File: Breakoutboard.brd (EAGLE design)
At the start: 17.7 x 25.4 mm, 3 parts

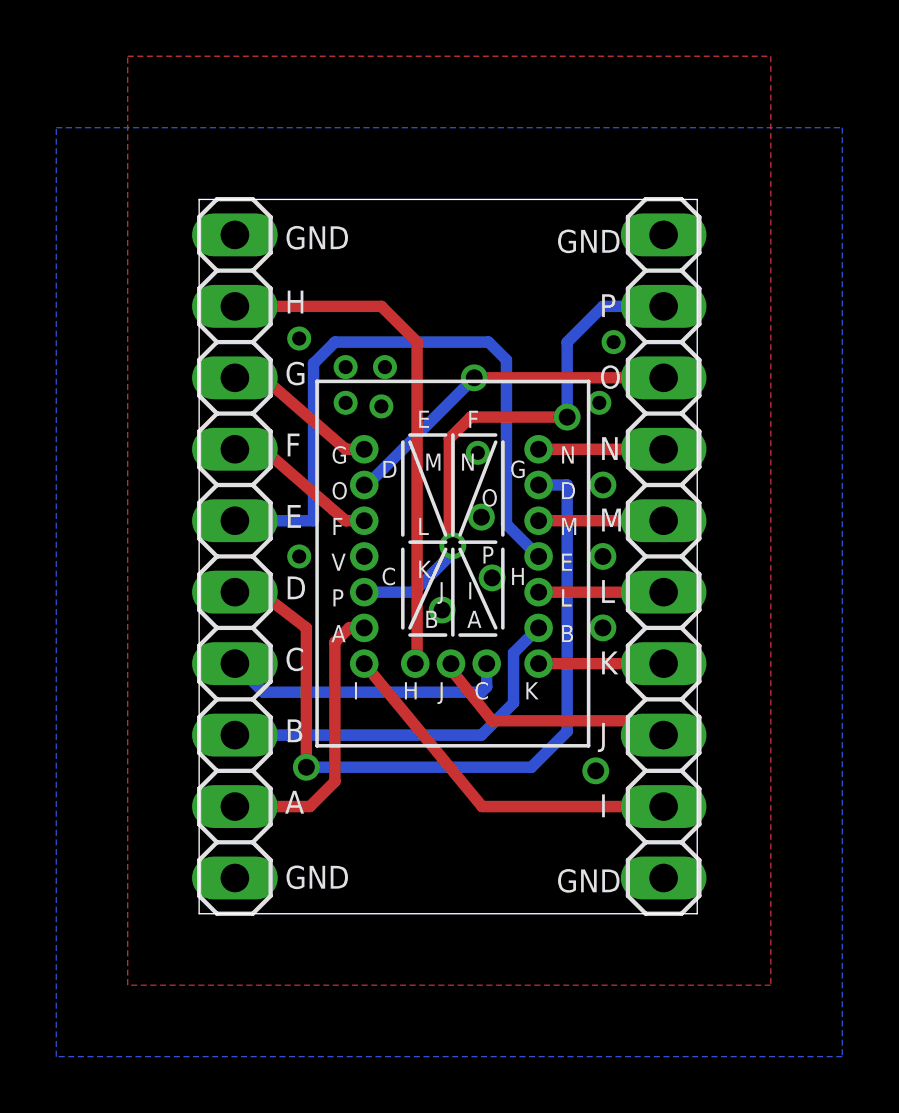
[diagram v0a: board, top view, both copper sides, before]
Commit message: wasn't quite centered yet
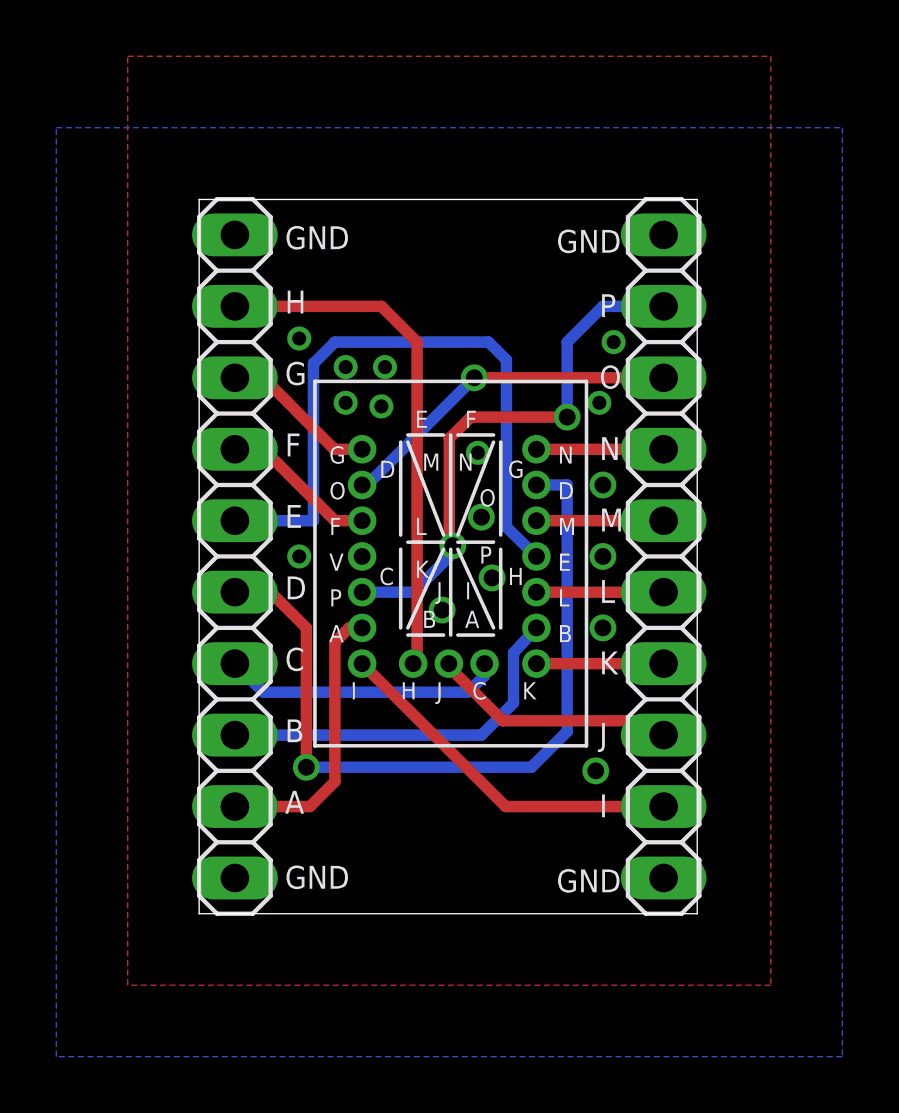
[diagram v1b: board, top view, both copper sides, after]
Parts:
- moved U$1 0.08 mm to (8.94, 11.9)
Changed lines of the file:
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@@
 <setting verticaltext="up"/>
 </settings>
-<grid distance="0.1" unitdist="inch" unit="inch" style="lines" multiple="1" display="yes" altdistance="0.005" altunitdist="inch" altunit="inch"/>
+<grid distance="0.1" unitdist="inch" unit="inch" style="lines" multiple="1" display="yes" altdistance="0.001" altunitdist="inch" altunit="inch"/>
 <layers>
 <layer number="1" name="Top" color="4" fill="1" visible="yes" active="yes"/>
@@
 </autorouter>
 <elements>
-<element name="U$1" library="KW-104AL" package="127" value="" x="9.017" y="11.938"/>
+<element name="U$1" library="KW-104AL" package="127" value="" x="8.9408" y="11.938"/>
 <element name="JP1" library="pinhead" package="1X10" value="" x="1.27" y="12.7" smashed="yes" rot="R270">
 <attribute name="VALUE" x="-1.905" y="25.4" size="1.27" layer="27" rot="R270"/>
@@
 <contactref element="JP1" pad="9"/>
 <contactref element="U$1" pad="A"/>
-<wire x1="5.8674" y1="10.16" x2="5.334" y2="10.16" width="0.4064" layer="1"/>
+<wire x1="5.7912" y1="10.16" x2="5.334" y2="10.16" width="0.4064" layer="1"/>
 <wire x1="5.334" y1="10.16" x2="4.826" y2="9.652" width="0.4064" layer="1"/>
 <wire x1="4.826" y1="9.652" x2="4.826" y2="4.699" width="0.4064" layer="1"/>
@@
 <wire x1="10.033" y1="6.35" x2="11.176" y2="7.493" width="0.4064" layer="16"/>
 <wire x1="11.176" y1="7.493" x2="11.176" y2="9.271" width="0.4064" layer="16"/>
-<wire x1="11.176" y1="9.271" x2="12.065" y2="10.16" width="0.4064" layer="16"/>
+<wire x1="11.176" y1="9.271" x2="11.9888" y2="10.16" width="0.4064" layer="16"/>
 </signal>
 <signal name="N$3">
 <contactref element="JP1" pad="7"/>
 <contactref element="U$1" pad="C"/>
-<wire x1="10.220959375" y1="8.89" x2="10.220959375" y2="8.061959375" width="0.4064" layer="16"/>
-<wire x1="10.220959375" y1="8.061959375" x2="10.033" y2="7.874" width="0.4064" layer="16"/>
-<wire x1="10.033" y1="7.874" x2="2.286" y2="7.874" width="0.4064" layer="16"/>
+<wire x1="10.144759375" y1="8.89" x2="10.144759375" y2="8.468359375" width="0.4064" layer="16"/>
+<wire x1="10.144759375" y1="8.468359375" x2="9.5504" y2="7.874" width="0.4064" layer="16"/>
+<wire x1="9.5504" y1="7.874" x2="2.286" y2="7.874" width="0.4064" layer="16"/>
 <wire x1="2.286" y1="7.874" x2="1.27" y2="8.89" width="0.4064" layer="16"/>
 </signal>
@@
 <contactref element="JP1" pad="6"/>
 <contactref element="U$1" pad="D"/>
-<wire x1="1.27" y1="11.43" x2="2.159" y2="11.43" width="0.4064" layer="1"/>
-<wire x1="2.159" y1="11.43" x2="3.81" y2="10.16" width="0.4064" layer="1"/>
+<wire x1="1.27" y1="11.43" x2="2.54" y2="11.43" width="0.4064" layer="1"/>
+<wire x1="2.54" y1="11.43" x2="3.81" y2="10.16" width="0.4064" layer="1"/>
 <wire x1="3.81" y1="10.16" x2="3.81" y2="5.207" width="0.4064" layer="1"/>
 <via x="3.81" y="5.207" extent="1-16" drill="0.6"/>
@@
 <wire x1="11.811" y1="5.207" x2="13.081" y2="6.477" width="0.4064" layer="16"/>
 <wire x1="13.081" y1="6.477" x2="13.081" y2="15.24" width="0.4064" layer="16"/>
-<wire x1="13.081" y1="15.24" x2="12.065" y2="15.24" width="0.4064" layer="16"/>
+<wire x1="13.081" y1="15.24" x2="11.9888" y2="15.24" width="0.4064" layer="16"/>
 </signal>
 <signal name="N$5">
@@
 <wire x1="4.826" y1="20.32" x2="10.287" y2="20.32" width="0.4064" layer="16"/>
 <wire x1="10.287" y1="20.32" x2="10.922" y2="19.685" width="0.4064" layer="16"/>
-<wire x1="10.922" y1="19.685" x2="10.922" y2="13.843" width="0.4064" layer="16"/>
-<wire x1="10.922" y1="13.843" x2="12.065" y2="12.7" width="0.4064" layer="16"/>
+<wire x1="10.922" y1="19.685" x2="10.922" y2="13.7414" width="0.4064" layer="16"/>
+<wire x1="10.922" y1="13.7414" x2="11.9888" y2="12.7" width="0.4064" layer="16"/>
 </signal>
 <signal name="N$6">
@@
 <contactref element="U$1" pad="F"/>
 <wire x1="1.27" y1="16.51" x2="2.286" y2="16.51" width="0.4064" layer="1"/>
-<wire x1="2.286" y1="16.51" x2="5.207" y2="13.97" width="0.4064" layer="1"/>
-<wire x1="5.207" y1="13.97" x2="5.8674" y2="13.97" width="0.4064" layer="1"/>
+<wire x1="2.286" y1="16.51" x2="4.826" y2="13.97" width="0.4064" layer="1"/>
+<wire x1="4.826" y1="13.97" x2="5.7912" y2="13.97" width="0.4064" layer="1"/>
 </signal>
 <signal name="N$7">
@@
 <contactref element="U$1" pad="G"/>
 <wire x1="1.27" y1="19.05" x2="2.286" y2="19.05" width="0.4064" layer="1"/>
-<wire x1="2.286" y1="19.05" x2="5.207" y2="16.51" width="0.4064" layer="1"/>
-<wire x1="5.207" y1="16.51" x2="5.8674" y2="16.51" width="0.4064" layer="1"/>
+<wire x1="2.286" y1="19.05" x2="4.8006" y2="16.51" width="0.4064" layer="1"/>
+<wire x1="4.8006" y1="16.51" x2="5.7912" y2="16.51" width="0.4064" layer="1"/>
 </signal>
 <signal name="N$8">
@@
 <wire x1="6.477" y1="21.59" x2="7.747" y2="20.32" width="0.4064" layer="1"/>
 <wire x1="7.747" y1="20.32" x2="7.747" y2="8.9560375" width="0.4064" layer="1"/>
-<wire x1="7.747" y1="8.9560375" x2="7.6809625" y2="8.89" width="0.4064" layer="1"/>
+<wire x1="7.747" y1="8.9560375" x2="7.6047625" y2="8.89" width="0.4064" layer="1"/>
 </signal>
 <signal name="N$9">
 <contactref element="JP2" pad="9"/>
 <contactref element="U$1" pad="I"/>
-<wire x1="16.51" y1="3.81" x2="10.0584" y2="3.81" width="0.4064" layer="1"/>
-<wire x1="10.0584" y1="3.81" x2="5.8674" y2="8.89" width="0.4064" layer="1"/>
+<wire x1="16.51" y1="3.81" x2="10.8966" y2="3.81" width="0.4064" layer="1"/>
+<wire x1="10.8966" y1="3.81" x2="5.7912" y2="8.89" width="0.4064" layer="1"/>
 </signal>
 <signal name="N$10">
 <contactref element="JP2" pad="8"/>
 <contactref element="U$1" pad="J"/>
-<wire x1="8.950959375" y1="8.89" x2="8.89" y2="8.763" width="0.4064" layer="1"/>
-<wire x1="8.89" y1="8.763" x2="10.414" y2="6.858" width="0.4064" layer="1"/>
-<wire x1="10.414" y1="6.858" x2="16.51" y2="6.858" width="0.4064" layer="1"/>
+<wire x1="8.874759375" y1="8.89" x2="8.89" y2="8.763" width="0.4064" layer="1"/>
+<wire x1="8.89" y1="8.763" x2="10.795" y2="6.858" width="0.4064" layer="1"/>
+<wire x1="10.795" y1="6.858" x2="16.51" y2="6.858" width="0.4064" layer="1"/>
 <wire x1="16.51" y1="6.858" x2="16.51" y2="6.35" width="0.4064" layer="1"/>
 </signal>
@@
 <contactref element="U$1" pad="K"/>
 <contactref element="JP2" pad="7"/>
-<wire x1="12.065" y1="8.89" x2="16.51" y2="8.89" width="0.4064" layer="1"/>
+<wire x1="11.9888" y1="8.89" x2="16.51" y2="8.89" width="0.4064" layer="1"/>
 </signal>
 <signal name="N$12">
 <contactref element="JP2" pad="6"/>
 <contactref element="U$1" pad="L"/>
-<wire x1="12.065" y1="11.43" x2="16.51" y2="11.43" width="0.4064" layer="1"/>
+<wire x1="11.9888" y1="11.43" x2="16.51" y2="11.43" width="0.4064" layer="1"/>
 </signal>
 <signal name="N$13">
 <contactref element="U$1" pad="M"/>
 <contactref element="JP2" pad="5"/>
-<wire x1="12.065" y1="13.97" x2="16.51" y2="13.97" width="0.4064" layer="1"/>
+<wire x1="11.9888" y1="13.97" x2="16.51" y2="13.97" width="0.4064" layer="1"/>
 </signal>
 <signal name="N$14">
 <contactref element="JP2" pad="4"/>
 <contactref element="U$1" pad="N"/>
-<wire x1="12.065" y1="16.51" x2="16.51" y2="16.51" width="0.4064" layer="1"/>
+<wire x1="11.9888" y1="16.51" x2="16.51" y2="16.51" width="0.4064" layer="1"/>
 </signal>
 <signal name="N$15">
 <contactref element="JP2" pad="3"/>
 <contactref element="U$1" pad="O"/>
-<wire x1="5.8674" y1="15.24" x2="5.969" y2="15.24" width="0.4064" layer="16"/>
+<wire x1="5.7912" y1="15.24" x2="5.969" y2="15.24" width="0.4064" layer="16"/>
 <wire x1="5.969" y1="15.24" x2="9.779" y2="19.05" width="0.4064" layer="16"/>
 <via x="9.779" y="19.05" extent="1-16" drill="0.6"/>
@@
 <wire x1="9.017" y1="13.081" x2="9.017" y2="12.827" width="0.4064" layer="16"/>
 <wire x1="9.017" y1="12.827" x2="7.62" y2="11.43" width="0.4064" layer="16"/>
-<wire x1="7.62" y1="11.43" x2="5.8674" y2="11.43" width="0.4064" layer="16"/>
+<wire x1="7.62" y1="11.43" x2="5.7912" y2="11.43" width="0.4064" layer="16"/>
 </signal>
 </signals>
